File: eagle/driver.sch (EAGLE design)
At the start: 96 parts, among them IC1 XMEGA128A1, IC10 ST95P08M, IC11 ST95P08M, IC12 ST95P08M, IC13 ST95P08M, IC14 ST95P08M, IC15 ST95P08M, IC16 74AHC1G02DBV, IC17 74AHC1G02DBV, IC18 74AHC1G125DBV, IC19 74AHC1G125DBV, IC2 74AC16244, IC20 ST95P08M, IC21 ST95P08M, IC22 ST95P08M, IC23 ST95P08M, IC24 ST95P08M, IC25 ST95P08M, IC3 74AC16244, IC4 74AC16244, IC5 74AC16244, IC6 74AC16374, IC7 74AC16374, IC8 74AC16374, IC9 74AC16374, SW1 FSM2JSMA

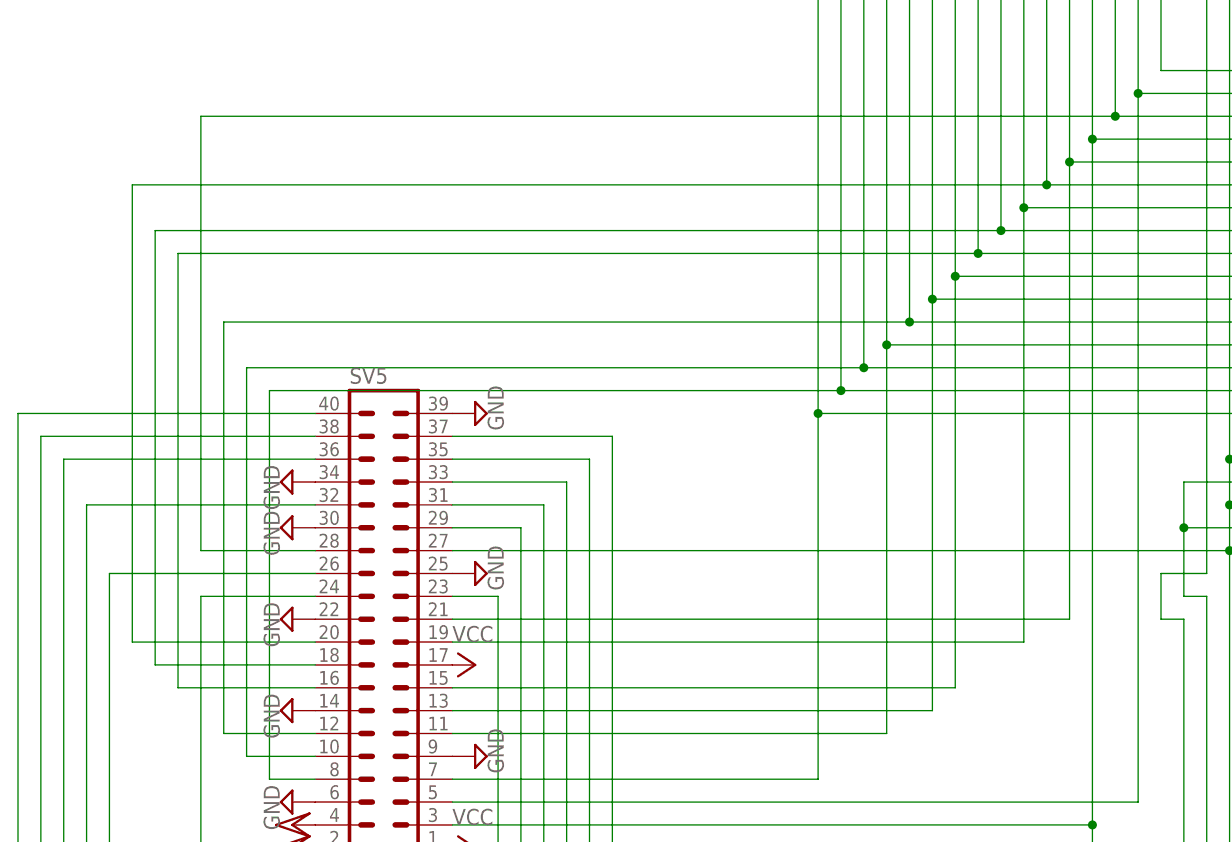
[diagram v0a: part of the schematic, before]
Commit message: fix pinout for rpi header
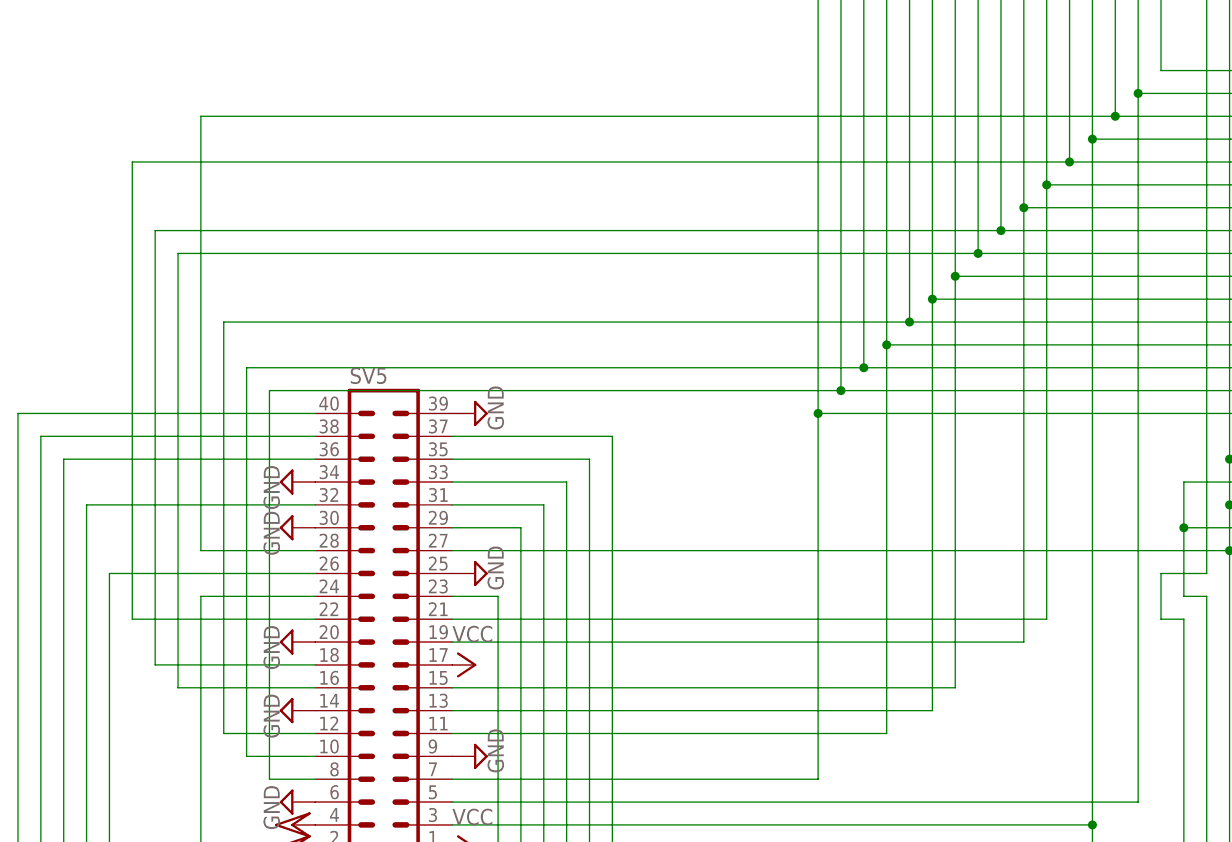
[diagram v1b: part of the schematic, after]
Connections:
- net GND: now also SV5.20; no longer SV5.22
- net N$30: now also SV5.22; no longer SV5.21
- net N$34: now also SV5.21; no longer SV5.20
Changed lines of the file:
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@@
 <attribute name="VALUE" x="-20.955" y="301.625" size="1.778" layer="96" rot="R270"/>
 </instance>
-<instance part="SUPPLY30" gate="GND" x="-17.78" y="309.88" smashed="yes" rot="R270">
-<attribute name="VALUE" x="-20.955" y="311.785" size="1.778" layer="96" rot="R270"/>
+<instance part="SUPPLY30" gate="GND" x="-17.78" y="307.34" smashed="yes" rot="R270">
+<attribute name="VALUE" x="-20.955" y="309.245" size="1.778" layer="96" rot="R270"/>
 </instance>
 <instance part="SUPPLY31" gate="GND" x="2.54" y="314.96" smashed="yes" rot="R90">
@@
 </segment>
 <segment>
-<pinref part="SV5" gate="G$1" pin="22"/>
 <pinref part="SUPPLY30" gate="GND" pin="GND"/>
+<pinref part="SV5" gate="G$1" pin="20"/>
 </segment>
 <segment>
@@
 <wire x1="68.58" y1="406.4" x2="68.58" y2="360.68" width="0.1524" layer="91"/>
 <wire x1="68.58" y1="360.68" x2="88.9" y2="360.68" width="0.1524" layer="91"/>
-<pinref part="SV5" gate="G$1" pin="21"/>
-<wire x1="0" y1="309.88" x2="68.58" y2="309.88" width="0.1524" layer="91"/>
-<wire x1="68.58" y1="309.88" x2="68.58" y2="360.68" width="0.1524" layer="91"/>
+<wire x1="-35.56" y1="309.88" x2="-35.56" y2="360.68" width="0.1524" layer="91"/>
+<pinref part="SV5" gate="G$1" pin="22"/>
+<wire x1="-15.24" y1="309.88" x2="-35.56" y2="309.88" width="0.1524" layer="91"/>
+<wire x1="68.58" y1="360.68" x2="-35.56" y2="360.68" width="0.1524" layer="91"/>
 <junction x="68.58" y="360.68"/>
 </segment>
@@
 <pinref part="IC6" gate="G$1" pin="2D3"/>
 <wire x1="66.04" y1="408.94" x2="88.9" y2="408.94" width="0.1524" layer="91"/>
-<pinref part="SV5" gate="G$1" pin="20"/>
-<wire x1="-15.24" y1="307.34" x2="-35.56" y2="307.34" width="0.1524" layer="91"/>
-<wire x1="-35.56" y1="307.34" x2="-35.56" y2="358.14" width="0.1524" layer="91"/>
-<wire x1="-35.56" y1="358.14" x2="66.04" y2="358.14" width="0.1524" layer="91"/>
+<pinref part="SV5" gate="G$1" pin="21"/>
+<wire x1="0" y1="309.88" x2="66.04" y2="309.88" width="0.1524" layer="91"/>
+<wire x1="66.04" y1="358.14" x2="66.04" y2="309.88" width="0.1524" layer="91"/>
 <junction x="66.04" y="358.14"/>
 </segment>

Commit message: add pull ups for register and buffer output enable lines
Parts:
- added R38, R39, R40, R41: 33k, rcl:R-US_R0402
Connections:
- net N$16: now also R41.1
- net N$19: now also R40.1
- net N$48: now also R38.2
- net N$56: now also R39.2
- net VCC: now also R38.1, R39.1, R40.2, R41.2
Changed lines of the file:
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@@
 <part name="SUPPLY114" library="supply2" library_urn="urn:adsk.eagle:library:372" deviceset="GND" device=""/>
 <part name="SUPPLY115" library="supply2" library_urn="urn:adsk.eagle:library:372" deviceset="GND" device=""/>
+<part name="R38" library="rcl" library_urn="urn:adsk.eagle:library:334" deviceset="R-US_" device="R0402" package3d_urn="urn:adsk.eagle:package:23547/3" value="33k"/>
+<part name="R39" library="rcl" library_urn="urn:adsk.eagle:library:334" deviceset="R-US_" device="R0402" package3d_urn="urn:adsk.eagle:package:23547/3" value="33k"/>
+<part name="R40" library="rcl" library_urn="urn:adsk.eagle:library:334" deviceset="R-US_" device="R0402" package3d_urn="urn:adsk.eagle:package:23547/3" value="33k"/>
+<part name="R41" library="rcl" library_urn="urn:adsk.eagle:library:334" deviceset="R-US_" device="R0402" package3d_urn="urn:adsk.eagle:package:23547/3" value="33k"/>
+<part name="P+74" library="supply1" library_urn="urn:adsk.eagle:library:371" deviceset="VCC" device=""/>
+<part name="P+75" library="supply1" library_urn="urn:adsk.eagle:library:371" deviceset="VCC" device=""/>
+<part name="P+76" library="supply1" library_urn="urn:adsk.eagle:library:371" deviceset="VCC" device=""/>
+<part name="P+77" library="supply1" library_urn="urn:adsk.eagle:library:371" deviceset="VCC" device=""/>
 </parts>
 <sheets>
@@
 <attribute name="VALUE" x="254.635" y="132.715" size="1.778" layer="96" rot="R90"/>
 </instance>
+<instance part="R38" gate="G$1" x="106.68" y="48.26" smashed="yes" rot="R270">
+<attribute name="NAME" x="108.1786" y="52.07" size="1.778" layer="95" rot="R270"/>
+<attribute name="VALUE" x="103.378" y="52.07" size="1.778" layer="96" rot="R270"/>
+</instance>
+<instance part="R39" gate="G$1" x="114.3" y="48.26" smashed="yes" rot="R270">
+<attribute name="NAME" x="115.7986" y="52.07" size="1.778" layer="95" rot="R270"/>
+<attribute name="VALUE" x="110.998" y="52.07" size="1.778" layer="96" rot="R270"/>
+</instance>
+<instance part="R40" gate="G$1" x="228.6" y="96.52" smashed="yes">
+<attribute name="NAME" x="224.79" y="98.0186" size="1.778" layer="95"/>
+<attribute name="VALUE" x="224.79" y="93.218" size="1.778" layer="96"/>
+</instance>
+<instance part="R41" gate="G$1" x="228.6" y="88.9" smashed="yes">
+<attribute name="NAME" x="224.79" y="90.3986" size="1.778" layer="95"/>
+<attribute name="VALUE" x="224.79" y="85.598" size="1.778" layer="96"/>
+</instance>
+<instance part="P+74" gate="VCC" x="106.68" y="55.88" smashed="yes">
+<attribute name="VALUE" x="104.14" y="53.34" size="1.778" layer="96" rot="R90"/>
+</instance>
+<instance part="P+75" gate="VCC" x="114.3" y="55.88" smashed="yes">
+<attribute name="VALUE" x="111.76" y="53.34" size="1.778" layer="96" rot="R90"/>
+</instance>
+<instance part="P+76" gate="VCC" x="236.22" y="96.52" smashed="yes" rot="R270">
+<attribute name="VALUE" x="233.68" y="99.06" size="1.778" layer="96"/>
+</instance>
+<instance part="P+77" gate="VCC" x="236.22" y="88.9" smashed="yes" rot="R270">
+<attribute name="VALUE" x="233.68" y="91.44" size="1.778" layer="96"/>
+</instance>
 </instances>
 <busses>
@@
 <pinref part="P+73" gate="VCC" pin="VCC"/>
 </segment>
+<segment>
+<pinref part="R38" gate="G$1" pin="1"/>
+<pinref part="P+74" gate="VCC" pin="VCC"/>
+</segment>
+<segment>
+<pinref part="R39" gate="G$1" pin="1"/>
+<pinref part="P+75" gate="VCC" pin="VCC"/>
+</segment>
+<segment>
+<pinref part="R40" gate="G$1" pin="2"/>
+<pinref part="P+76" gate="VCC" pin="VCC"/>
+</segment>
+<segment>
+<pinref part="R41" gate="G$1" pin="2"/>
+<pinref part="P+77" gate="VCC" pin="VCC"/>
+</segment>
 </net>
 <net name="VCC/2" class="0">
@@
 <wire x1="223.52" y1="236.22" x2="220.98" y2="236.22" width="0.1524" layer="91"/>
 <pinref part="IC1" gate="G$1" pin="PE5"/>
-<wire x1="220.98" y1="228.6" x2="220.98" y2="66.04" width="0.1524" layer="91"/>
+<wire x1="220.98" y1="228.6" x2="220.98" y2="88.9" width="0.1524" layer="91"/>
+<wire x1="220.98" y1="88.9" x2="220.98" y2="66.04" width="0.1524" layer="91"/>
 <wire x1="220.98" y1="66.04" x2="198.12" y2="66.04" width="0.1524" layer="91"/>
 <junction x="220.98" y="228.6"/>
@@
 <wire x1="218.44" y1="309.88" x2="218.44" y2="320.04" width="0.1524" layer="91"/>
 <junction x="218.44" y="320.04"/>
+<pinref part="R41" gate="G$1" pin="1"/>
+<wire x1="223.52" y1="88.9" x2="220.98" y2="88.9" width="0.1524" layer="91"/>
+<junction x="220.98" y="88.9"/>
 </segment>
 </net>
@@
 <pinref part="IC1" gate="G$1" pin="PE6"/>
 <wire x1="198.12" y1="68.58" x2="218.44" y2="68.58" width="0.1524" layer="91"/>
-<wire x1="218.44" y1="165.1" x2="218.44" y2="68.58" width="0.1524" layer="91"/>
+<wire x1="218.44" y1="165.1" x2="218.44" y2="96.52" width="0.1524" layer="91"/>
 <junction x="218.44" y="165.1"/>
+<wire x1="218.44" y1="96.52" x2="218.44" y2="68.58" width="0.1524" layer="91"/>
 <wire x1="218.44" y1="172.72" x2="218.44" y2="307.34" width="0.1524" layer="91"/>
 <wire x1="218.44" y1="307.34" x2="223.52" y2="307.34" width="0.1524" layer="91"/>
@@
 <wire x1="220.98" y1="312.42" x2="220.98" y2="383.54" width="0.1524" layer="91"/>
 <junction x="220.98" y="383.54"/>
+<pinref part="R40" gate="G$1" pin="1"/>
+<wire x1="223.52" y1="96.52" x2="218.44" y2="96.52" width="0.1524" layer="91"/>
+<junction x="218.44" y="96.52"/>
 </segment>
 </net>
@@
 <pinref part="IC1" gate="G$1" pin="PK4"/>
 <wire x1="83.82" y1="228.6" x2="83.82" y2="40.64" width="0.1524" layer="91"/>
-<wire x1="83.82" y1="40.64" x2="144.78" y2="40.64" width="0.1524" layer="91"/>
+<wire x1="83.82" y1="40.64" x2="114.3" y2="40.64" width="0.1524" layer="91"/>
 <junction x="83.82" y="228.6"/>
+<wire x1="114.3" y1="40.64" x2="144.78" y2="40.64" width="0.1524" layer="91"/>
 <wire x1="83.82" y1="233.68" x2="83.82" y2="312.42" width="0.1524" layer="91"/>
 <junction x="83.82" y="233.68"/>
@@
 <wire x1="81.28" y1="312.42" x2="81.28" y2="320.04" width="0.1524" layer="91"/>
 <junction x="81.28" y="320.04"/>
+<pinref part="R39" gate="G$1" pin="2"/>
+<wire x1="114.3" y1="43.18" x2="114.3" y2="40.64" width="0.1524" layer="91"/>
+<junction x="114.3" y="40.64"/>
 </segment>
 </net>
@@
 <wire x1="88.9" y1="170.18" x2="81.28" y2="170.18" width="0.1524" layer="91"/>
 <pinref part="IC1" gate="G$1" pin="PK3"/>
-<wire x1="144.78" y1="38.1" x2="81.28" y2="38.1" width="0.1524" layer="91"/>
+<wire x1="144.78" y1="38.1" x2="106.68" y2="38.1" width="0.1524" layer="91"/>
+<wire x1="106.68" y1="38.1" x2="81.28" y2="38.1" width="0.1524" layer="91"/>
 <wire x1="81.28" y1="38.1" x2="81.28" y2="165.1" width="0.1524" layer="91"/>
 <junction x="81.28" y="165.1"/>
@@
 <wire x1="83.82" y1="314.96" x2="83.82" y2="383.54" width="0.1524" layer="91"/>
 <junction x="83.82" y="383.54"/>
+<pinref part="R38" gate="G$1" pin="2"/>
+<wire x1="106.68" y1="43.18" x2="106.68" y2="38.1" width="0.1524" layer="91"/>
+<junction x="106.68" y="38.1"/>
 </segment>
 </net>

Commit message: consolidate duplicate signals on board
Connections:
- net N$16 renamed OEN1
- net N$19 renamed OEN0
- removed net CLK_EN0: IC1.PK5, IC19A.OE
- removed net CLK_EN1: IC1.PK6, IC18A.OE
- removed net N$48: IC1.PK3, IC6G$1.1OE, IC6G$1.2OE, IC9G$1.1OE, IC9G$1.2OE, R38.2
- removed net N$56: IC1.PK4, IC7G$1.1OE, IC7G$1.2OE, IC8G$1.1OE, IC8G$1.2OE, R39.2
- removed net VSYNC2: IC1.PA6, IC20G$1.!S, IC21G$1.!S, IC22G$1.!S, IC8G$1.2Q5
- removed net VSYNC3: IC1.PA7, IC23G$1.!S, IC24G$1.!S, IC25G$1.!S, IC9G$1.1Q4
- new net IEN0: IC1.PK3, IC19A.OE, IC6G$1.1OE, IC6G$1.2OE, IC9G$1.1OE, IC9G$1.2OE, R38.2
- new net IEN1: IC1.PK4, IC18A.OE, IC7G$1.1OE, IC7G$1.2OE, IC8G$1.1OE, IC8G$1.2OE, R39.2
- net GND: now also IC8G$1.2D5, IC9G$1.1D4
- net N$94: no longer IC8G$1.2D5, IC9G$1.1D4
- net VSYNC0: now also IC23G$1.!S, IC24G$1.!S, IC25G$1.!S
- net VSYNC1: now also IC20G$1.!S, IC21G$1.!S, IC22G$1.!S

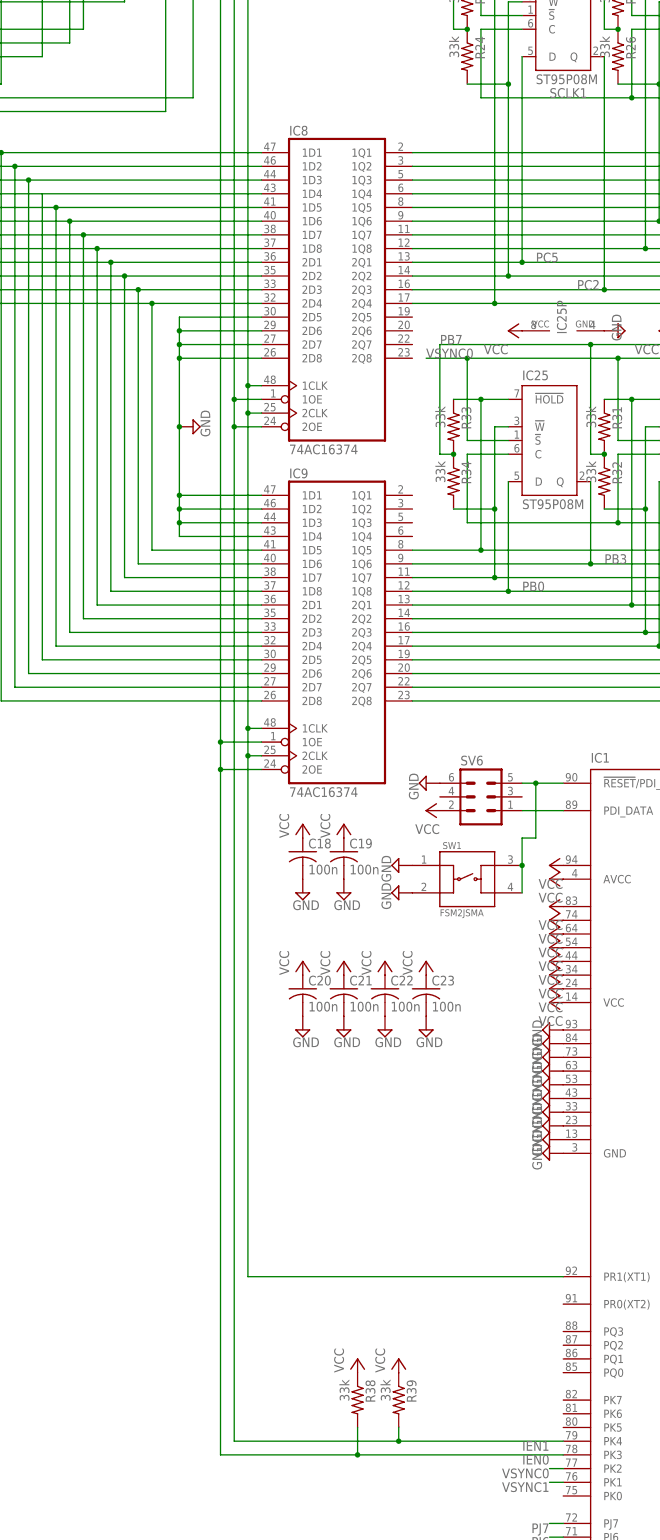
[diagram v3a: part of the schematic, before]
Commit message: fix sram chip select pins
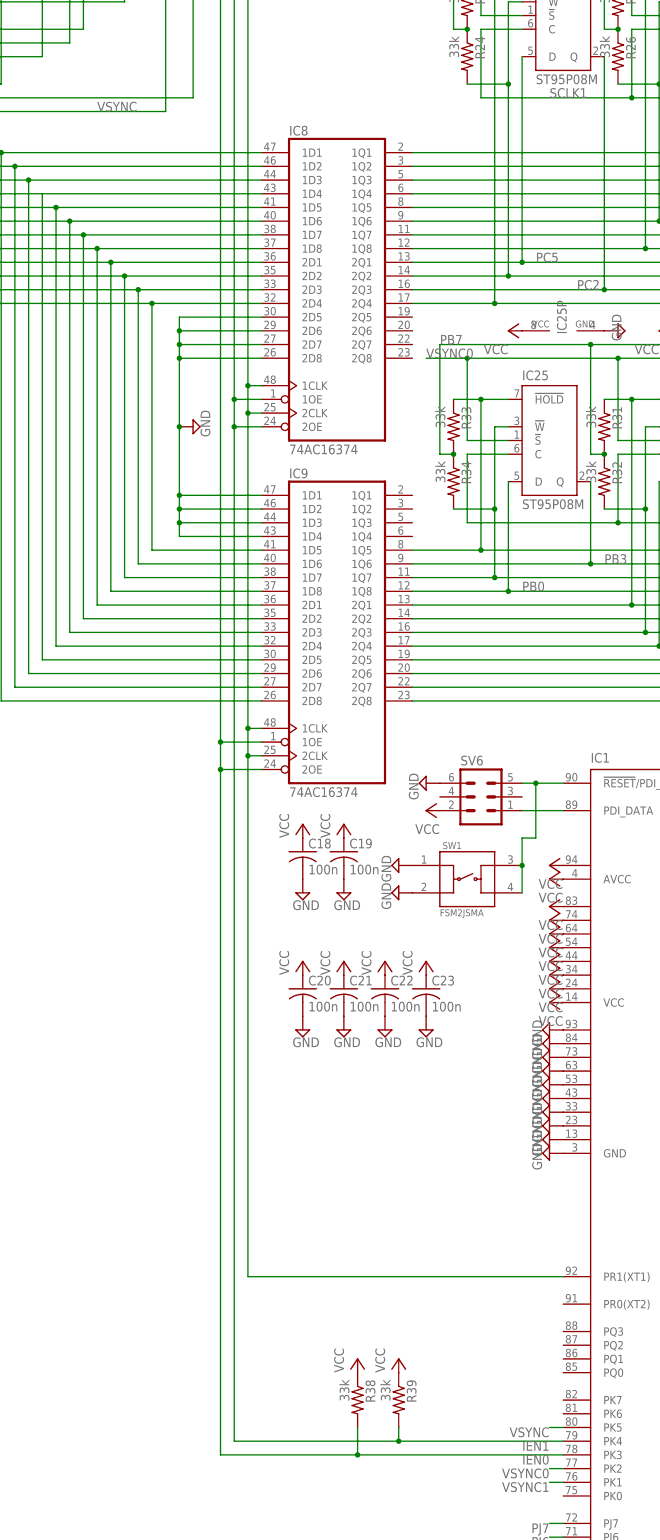
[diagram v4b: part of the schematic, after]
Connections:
- removed net N$94: IC6G$1.2D5, IC7G$1.1D4, SV5.3
- new net VSYNC: IC1.PK5, IC6G$1.2D5, IC7G$1.1D4, SV5.3
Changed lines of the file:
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@@
 </segment>
 </net>
-<net name="N$94" class="0">
+<net name="VSYNC" class="0">
 <segment>
 <pinref part="IC6" gate="G$1" pin="2D5"/>
@@
 <wire x1="71.12" y1="287.02" x2="71.12" y2="363.22" width="0.1524" layer="91"/>
 <junction x="71.12" y="363.22"/>
+<label x="58.42" y="287.02" size="1.778" layer="95"/>
+</segment>
+<segment>
+<pinref part="IC1" gate="G$1" pin="PK5"/>
+<wire x1="144.78" y1="43.18" x2="142.24" y2="43.18" width="0.1524" layer="91"/>
+<label x="142.24" y="43.18" size="1.778" layer="95" rot="R180"/>
 </segment>
 </net>
